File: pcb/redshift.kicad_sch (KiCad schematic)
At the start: 41 parts, among them IC1 LPC5516JEV98, J1 USB_C_Receptacle_USB2.0, J2 Side, J3 Conn_01x06_Female, SW1 SW_SPDT, SW2 SW_SPDT, SW3 SW_SPD, U1 PAW 3399, U2 MIC5350-SGYMT-TR

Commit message: pre v0.1
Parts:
- removed U1: PAW 3399, openinput:PXI-DIP-16, symbol openinput:PMW3389DM‐T3QU
- removed U2: MIC5350-SGYMT-TR, Package_DFN_QFN:Micrel_MLF-8-1EP_2x2mm_P0.5mm_EP0.8x1.3mm_ThermalVias, symbol Regulator_Linear:MIC5356-SGYMME
- added C17, C19, C21, C24: 100nF, Capacitor_SMD:C_0402_1005Metric, symbol Device:C_Small
- added C18, C22: 4.7uF, Capacitor_SMD:C_0402_1005Metric, symbol Device:C_Small
- added C20: 33uF, Capacitor_SMD:C_0402_1005Metric, symbol Device:C_Small
- added C23: 0.1uF, Capacitor_SMD:C_0201_0603Metric, symbol Device:C_Small
- added R10, R11, R12, R8, R9: 10k, Resistor_SMD:R_0402_1005Metric, symbol Device:R_Small
- added TP1, TP10, TP11, TP12, TP13, TP14, TP15, TP16, TP17, TP2, TP3, TP4, TP5, TP6, TP7, TP8, TP9: TestPoint, TestPoint:TestPoint_Pad_D1.5mm, symbol Connector:TestPoint
- added U1: PAW3399DM‐T4QU, openinput:PXI-DIP-16, symbol openinput:PAW3399DM‐T4QU
- added U3: TCR2LE19,LM(CT, Package_TO_SOT_SMD:SOT-553, symbol Regulator_Linear:TLV70012_SOT353
- added U4: MIC5528-3.3YMT-TR, MIC5528-3:SON40P120X120X60-7N, symbol Regulator_Linear:MIC5504-3.3YM5
- added Y1: XRCGB16M000FXN16R0, Crystal:Crystal_SMD_2016-4Pin_2.0x1.6mm, symbol Device:Crystal_GND2
- C10: value 0.1uF -> 2.2uF
- C15: value 100nF -> 0.1uF; footprint Capacitor_SMD:C_0402_1005Metric -> Capacitor_SMD:C_0201_0603Metric
- C2, C7: value 2.2uF -> 0.1uF
- J3: now left out of the parts list
- SW1, SW2: value SW_SPDT -> SW_SP
- SW3: value SW_SPD -> SW_SP
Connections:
- net BYP is gone; now on net +3V3: C10.1
- net +1V8: now also C19.2, C20.2, TP16.1, U3.3 (OUT)
- net +3V3: now also C17.1, C18.1, C24.1, R10.2, R11.2, R9.2, TP12.1, U4.1 (VOUT), U4.2 (VOUT); no longer C15.1, C8.1
- net +5V: now also C8.1, TP17.1, U3.1 (EN), U3.4 (NC), U4.4 (EN), U4.6 (VIN)
- net ENC_A: now also TP13.1
- net ENC_B: now also TP15.1
- net FC6_CS1: now also U1.13 (~{CS})
- net FC6_MISO: now also R8.2, TP5.1, U1.12 (MISO)
- net FC6_MOSI: now also TP3.1, U1.11 (MOSI)
- net FC6_SCK: now also TP1.1, U1.10 (SCLK)
- net GND: now also C21.2, C22.2, C23.2, C24.2, R12.2, R8.1, TP14.1, U1.3 (GND), U1.8 (GND), U3.2 (GND), U4.3 (GND); no longer IC1.N3 (XTAL32M_P)
- net RESET: now also R9.1
- net SNSR_LED: now also U1.15 (LED_P)
- net SNSR_RST: now also U1.14 (~{RESET})
- net SW1_L_NC: now also TP4.1
- net SW1_L_NO: now also TP2.1
- net SW2_R_NC: now also TP7.1
- net SW2_R_NO: now also TP6.1
- net SW3_M_NC: now also TP11.1
- net SW3_M_NO: now also TP10.1
- net SWCLK: now also R12.1
- net SWDIO: now also R10.1
- net SWO: now also R11.1
- net USB_D+: now also D1.3 (I/O2), TP8.1; no longer D1.2 (I/O1)
- net USB_D-: now also D1.2 (I/O1), TP9.1; no longer D1.3 (I/O2)
- net XTAL-: now also C23.1, Y1.3
- net SNSR_MTN: now reaches IC1.E6 (PIO0_19)
- net SNSR_MTN: now also U1.9 (MOTION)
- new net: C17.2, C18.2, U1.7 (VDDIO)
- new net: C19.1, C20.1, U1.4 (VDD)
- new net: C21.1, C22.1, U1.5 (VDDPIX)
- new net XTAL+: C15.1, IC1.N3 (XTAL32M_P), Y1.1
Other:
- moved on the sheet: C16, C3, C4, C5, C6, C9, D2, D3, D4, D5, J2, J3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

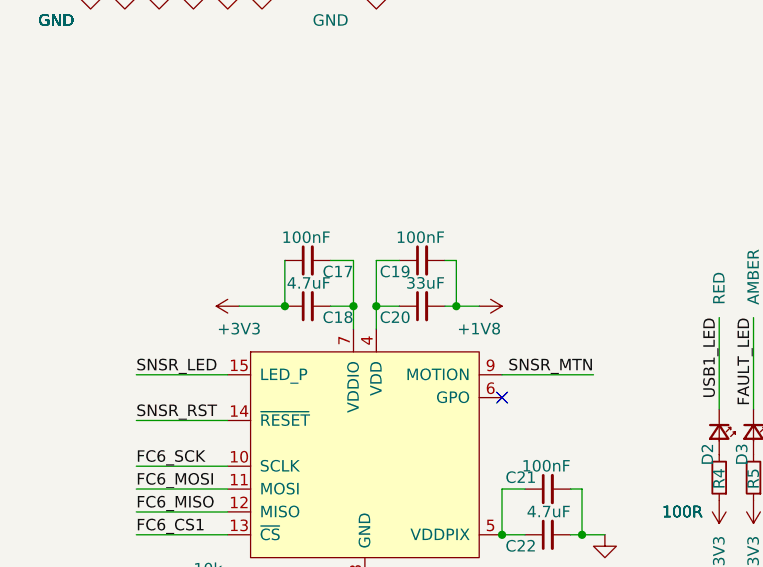
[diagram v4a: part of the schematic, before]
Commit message: add lpc55 footprint from solokeys, release v0.1
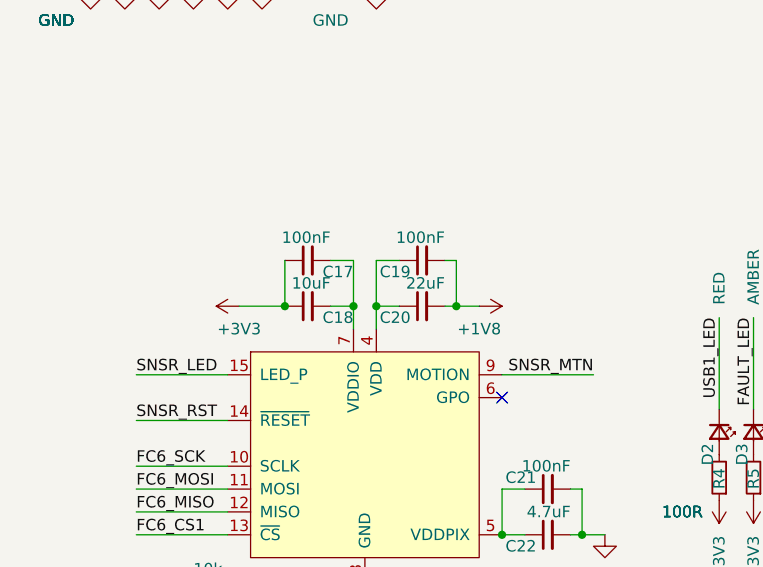
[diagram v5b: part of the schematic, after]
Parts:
- C18: value 4.7uF -> 10uF
- C20: value 33uF -> 22uF

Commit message: add ISP pin
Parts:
- added TP18: TestPoint, TestPoint:TestPoint_Pad_D1.5mm, symbol Connector:TestPoint
- C15, C23: value 0.1uF -> 12pF
- R4, R5, R6, R7: value 100R -> 10k
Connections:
- net ISP: now reaches IC1.A7 (PIO0_5/TDI)
- net ISP: now also TP18.1
- no-connect marks 66 -> 65

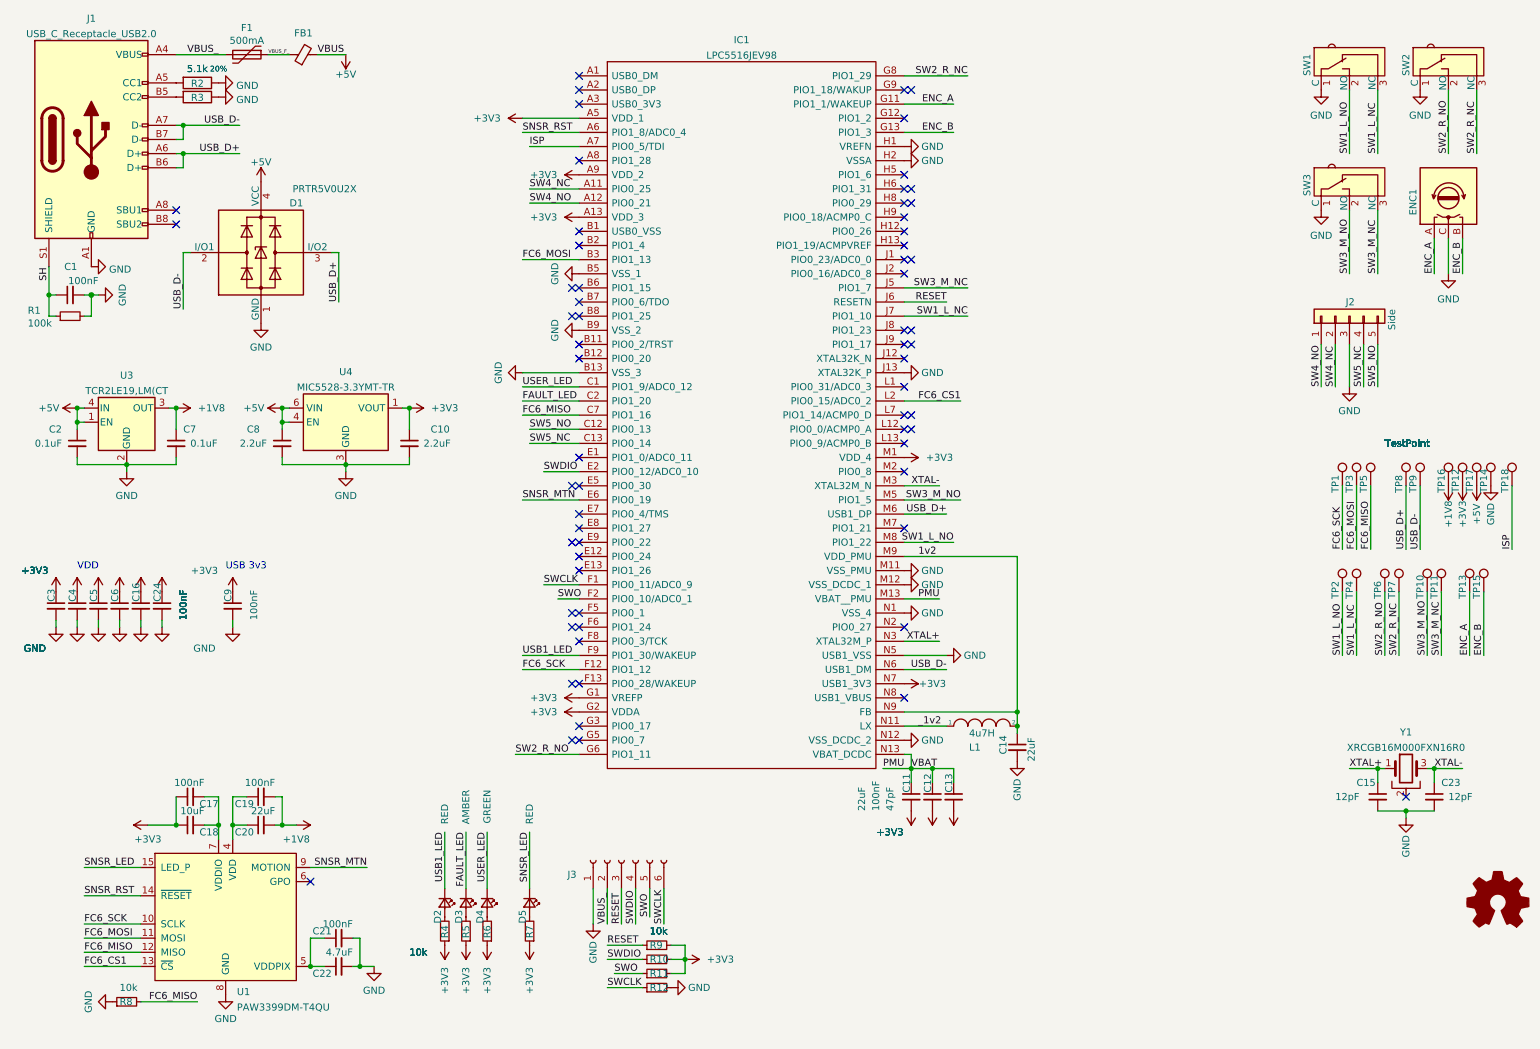
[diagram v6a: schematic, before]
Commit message: fix #2, add missing lib source
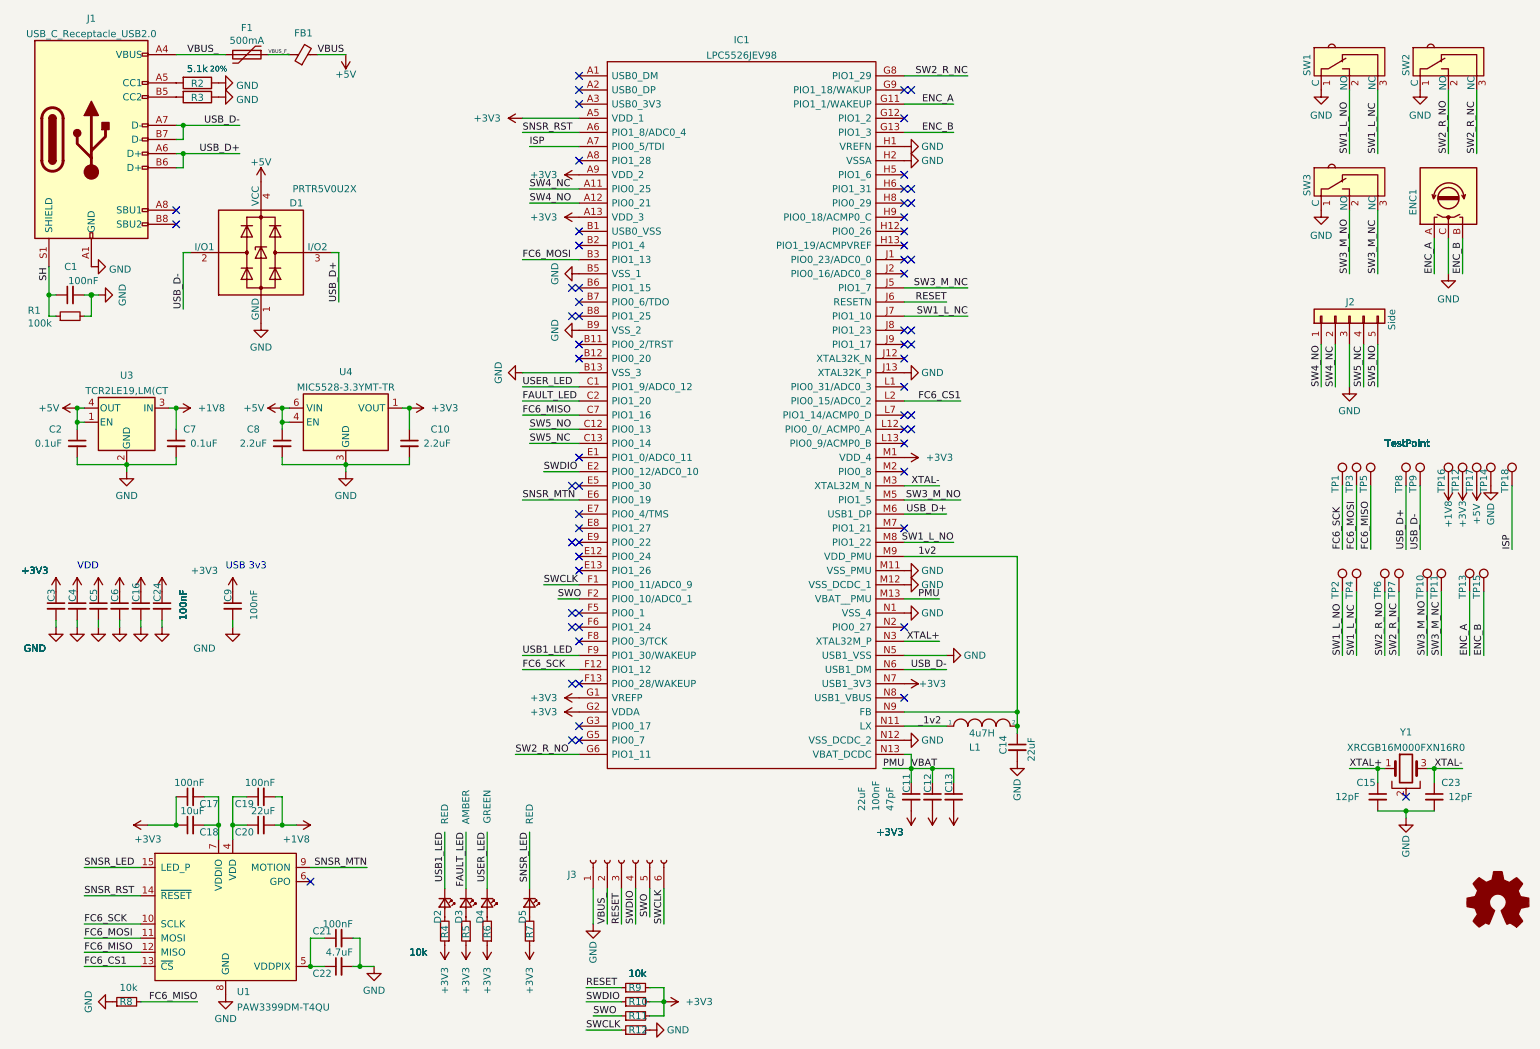
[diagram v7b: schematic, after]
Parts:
- C15, C23: footprint Capacitor_SMD:C_0201_0603Metric -> Capacitor_SMD:C_0402_1005Metric
- IC1: value LPC5516JEV98 -> LPC5526JEV98; footprint dekanova:BGA98C50P13X13_700X700X97 -> solokeys:BGA98C50P13X13_700X700X97N; symbol LPC5516JEV98:LPC5516JEV98 -> LPC5528JEV98K:LPC5528JEV98K; Manufacturer_Part_Number LPC5516JEV98 -> LPC5528JEV98K; Mouser Part Number (none) -> 771-LPC5528JEV98K; Mouser Price/Stock (none) -> https://www.mouser.co.uk/ProductDetail/NXP-Semiconductors/L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
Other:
- moved on the sheet: R10, R11, R12, R9

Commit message: update USB footprint, remove pad inside SWDIO trace
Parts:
- J1: footprint dekanova:GCT_USB4105-GF-A -> GCT_USB:GCT_USB4105-GF-A
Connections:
- net SH: now also J1.S2 (SHIELD), J1.S3 (SHIELD), J1.S4 (SHIELD)
